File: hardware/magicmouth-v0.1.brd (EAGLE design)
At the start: 100 x 80 mm, 36 parts, among them IC1 LM386N, IC2 ATMEGA328P_PDIP, J2 AUDIO-JACK2PTH, Q1 16Mhz, U1 ARDUINOR3-NOIOREF-NOTEXT

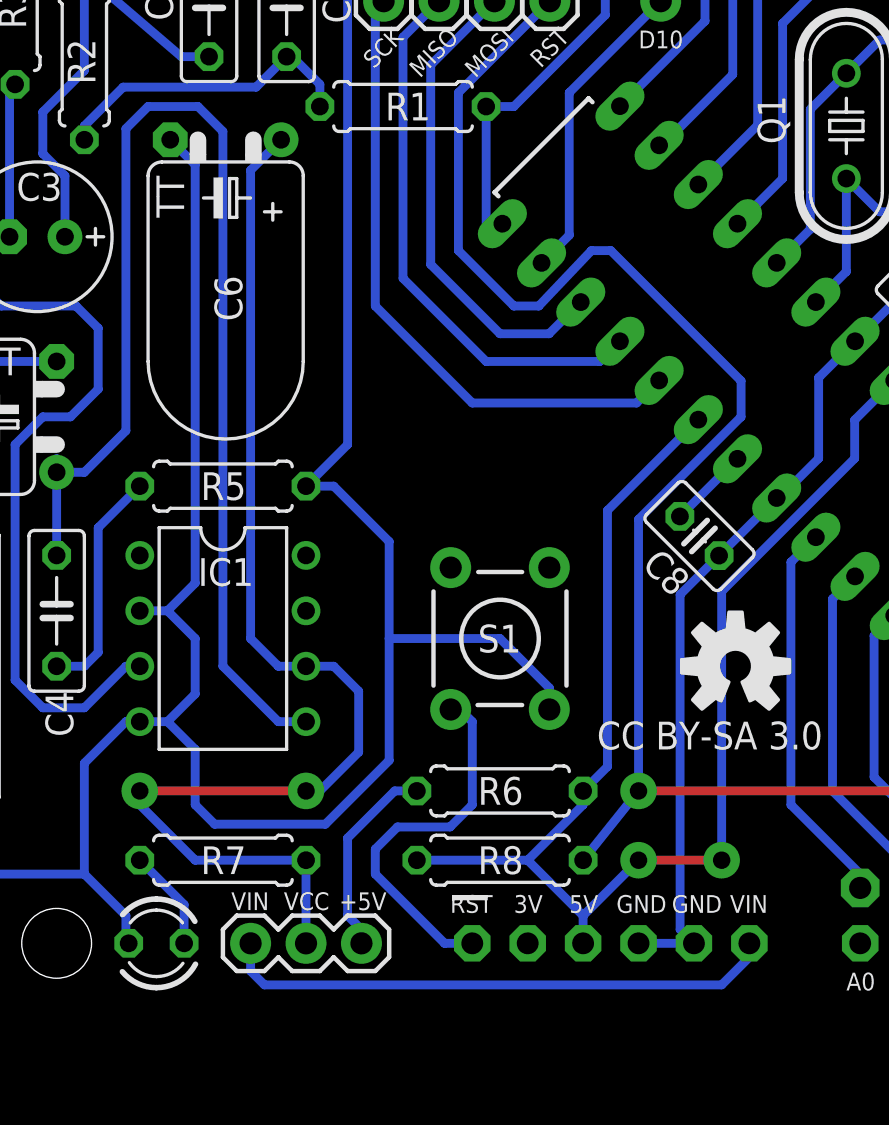
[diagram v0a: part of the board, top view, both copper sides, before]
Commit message: v0.1 and v1.0 eagle files
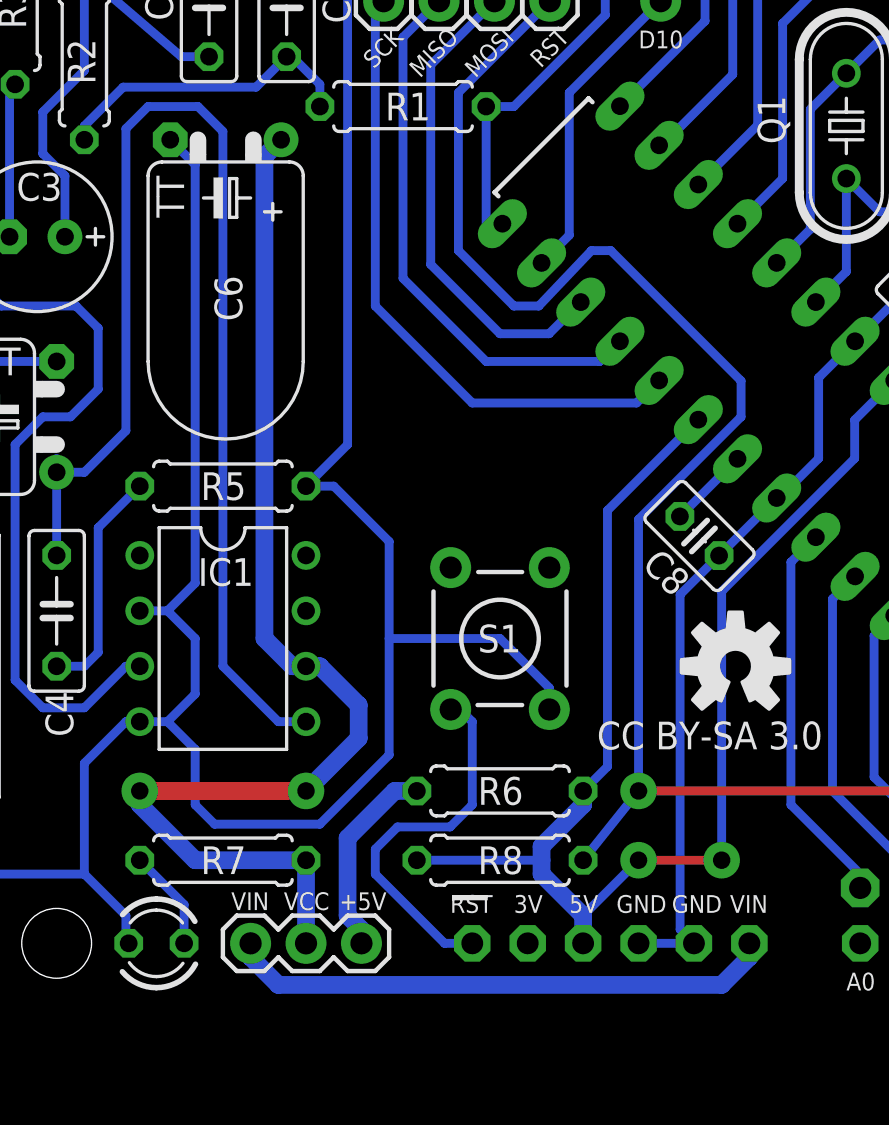
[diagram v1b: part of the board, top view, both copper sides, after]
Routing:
- net VCC: track 56.1 -> 54.4 mm
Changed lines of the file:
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@@
 <setting verticaltext="up"/>
 </settings>
-<grid distance="0.025" unitdist="inch" unit="mm" style="lines" multiple="1" display="yes" altdistance="0.025" altunitdist="inch" altunit="inch"/>
+<grid distance="25" unitdist="mil" unit="mil" style="lines" multiple="1" display="yes" altdistance="0.025" altunitdist="inch" altunit="inch"/>
 <layers>
 <layer number="1" name="Top" color="4" fill="1" visible="yes" active="yes"/>
@@
 <wire x1="27.305" y1="12.827" x2="27.432" y2="12.7" width="0.4064" layer="16"/>
 <wire x1="25.4" y1="15.875" x2="25.4" y2="20.955" width="0.4064" layer="16"/>
-<wire x1="36.449" y1="18.161" x2="39.37" y2="21.082" width="0.4064" layer="16"/>
+<wire x1="36.195" y1="18.161" x2="39.37" y2="21.336" width="0.4064" layer="16"/>
 <contactref element="R4" pad="A"/>
 <wire x1="27.305" y1="22.86" x2="27.94" y2="22.86" width="0.4064" layer="16"/>
@@
 <wire x1="30.48" y1="21.59" x2="30.48" y2="19.05" width="0.4064" layer="16"/>
 <wire x1="30.48" y1="19.05" x2="31.369" y2="18.161" width="0.4064" layer="16"/>
-<wire x1="31.369" y1="18.161" x2="36.449" y2="18.161" width="0.4064" layer="16"/>
+<wire x1="31.369" y1="18.161" x2="36.195" y2="18.161" width="0.4064" layer="16"/>
 <wire x1="25.4" y1="20.955" x2="27.305" y2="22.86" width="0.4064" layer="16"/>
 <contactref element="J1" pad="2"/>
@@
 <wire x1="36.83" y1="33.655" x2="39.37" y2="31.115" width="0.4064" layer="16"/>
 <wire x1="39.37" y1="31.115" x2="39.37" y2="26.67" width="0.4064" layer="16"/>
-<wire x1="39.37" y1="26.67" x2="39.37" y2="21.082" width="0.4064" layer="16"/>
+<wire x1="39.37" y1="26.67" x2="39.37" y2="21.336" width="0.4064" layer="16"/>
 <wire x1="35.56" y1="33.655" x2="35.433" y2="33.655" width="0.4064" layer="16"/>
 <wire x1="35.433" y1="33.655" x2="35.306" y2="33.782" width="0.4064" layer="16"/>
@@
 <contactref element="IC1" pad="6"/>
 <contactref element="C6" pad="+"/>
-<wire x1="36.83" y1="25.4" x2="35.56" y2="25.4" width="0.4064" layer="16"/>
-<wire x1="33.02" y1="48.133" x2="33.02" y2="26.67" width="0.4064" layer="16"/>
-<wire x1="33.02" y1="26.67" x2="34.29" y2="25.4" width="0.4064" layer="16"/>
-<wire x1="34.29" y1="25.4" x2="35.56" y2="25.4" width="0.4064" layer="16"/>
-<wire x1="37.973" y1="24.257" x2="36.83" y2="25.4" width="0.4064" layer="16"/>
-<wire x1="37.973" y1="24.257" x2="37.973" y2="21.463" width="0.4064" layer="16"/>
-<wire x1="35.56" y1="19.685" x2="36.195" y2="19.685" width="0.4064" layer="16"/>
-<wire x1="36.195" y1="19.685" x2="37.973" y2="21.463" width="0.4064" layer="16"/>
 <contactref element="R7" pad="2"/>
-<wire x1="30.48" y1="16.51" x2="27.94" y2="19.05" width="0.4064" layer="16"/>
-<wire x1="30.48" y1="16.51" x2="35.56" y2="16.51" width="0.4064" layer="16"/>
-<wire x1="35.56" y1="19.685" x2="27.94" y2="19.685" width="0.4064" layer="1"/>
-<wire x1="27.94" y1="19.685" x2="27.94" y2="19.05" width="0.4064" layer="16"/>
 <via x="35.56" y="19.685" extent="1-16" drill="0.8" diameter="1.6764"/>
 <via x="27.94" y="19.685" extent="1-16" drill="0.8" diameter="1.6764"/>
 <contactref element="JP1" pad="2"/>
-<wire x1="35.56" y1="12.7" x2="35.56" y2="16.51" width="0.4064" layer="16"/>
-<wire x1="33.02" y1="48.133" x2="34.417" y2="49.53" width="0.4064" layer="16"/>
+<wire x1="35.56" y1="25.4" x2="36.195" y2="25.4" width="0.8128" layer="16"/>
+<wire x1="36.195" y1="25.4" x2="37.973" y2="23.622" width="0.8128" layer="16"/>
+<wire x1="37.973" y1="23.622" x2="37.973" y2="22.098" width="0.8128" layer="16"/>
+<wire x1="37.973" y1="22.098" x2="35.56" y2="19.685" width="0.8128" layer="16"/>
+<wire x1="35.56" y1="12.7" x2="35.56" y2="16.51" width="0.8128" layer="16"/>
+<wire x1="35.56" y1="16.51" x2="30.48" y2="16.51" width="0.8128" layer="16"/>
+<wire x1="30.48" y1="16.51" x2="27.94" y2="19.05" width="0.8128" layer="16"/>
+<wire x1="27.94" y1="19.05" x2="27.94" y2="19.685" width="0.8128" layer="16"/>
+<wire x1="27.94" y1="19.685" x2="35.56" y2="19.685" width="0.8128" layer="1"/>
+<wire x1="35.56" y1="25.4" x2="34.925" y2="25.4" width="0.8128" layer="16"/>
+<wire x1="34.925" y1="25.4" x2="33.655" y2="26.67" width="0.8128" layer="16"/>
+<wire x1="33.655" y1="26.67" x2="33.655" y2="48.768" width="0.8128" layer="16"/>
+<wire x1="33.655" y1="48.768" x2="34.417" y2="49.53" width="0.8128" layer="16"/>
 </signal>
 <signal name="N$7">
 <contactref element="R6" pad="1"/>
-<wire x1="38.1" y1="13.335" x2="37.465" y2="13.97" width="0.4064" layer="16"/>
-<wire x1="37.465" y1="13.97" x2="37.465" y2="17.526" width="0.4064" layer="16"/>
-<wire x1="37.465" y1="17.526" x2="39.624" y2="19.685" width="0.4064" layer="16"/>
-<wire x1="39.624" y1="19.685" x2="40.64" y2="19.685" width="0.4064" layer="16"/>
 <contactref element="JP1" pad="1"/>
-<wire x1="38.1" y1="12.7" x2="38.1" y2="13.335" width="0.4064" layer="16"/>
+<wire x1="38.1" y1="12.7" x2="38.1" y2="13.335" width="0.8128" layer="16"/>
+<wire x1="38.1" y1="13.335" x2="37.465" y2="13.97" width="0.8128" layer="16"/>
+<wire x1="37.465" y1="13.97" x2="37.465" y2="17.526" width="0.8128" layer="16"/>
+<wire x1="37.465" y1="17.526" x2="39.624" y2="19.685" width="0.8128" layer="16"/>
+<wire x1="39.624" y1="19.685" x2="40.64" y2="19.685" width="0.8128" layer="16"/>
 </signal>
 <signal name="N$10">
@@
 <wire x1="54.61" y1="28.829" x2="60.706" y2="34.925" width="0.4064" layer="16"/>
 <wire x1="60.706" y1="34.925" x2="60.706" y2="36.68495" width="0.4064" layer="16"/>
-<wire x1="48.26" y1="12.7" x2="48.26" y2="13.97" width="0.4064" layer="16"/>
 <wire x1="48.26" y1="13.97" x2="50.8" y2="16.51" width="0.4064" layer="16"/>
 <wire x1="50.8" y1="16.51" x2="54.61" y2="16.51" width="0.4064" layer="1"/>
@@
 <via x="50.8" y="16.51" extent="1-16" drill="0.8" diameter="1.6764"/>
 <via x="54.61" y="16.51" extent="1-16" drill="0.8" diameter="1.6764"/>
-<wire x1="45.72" y1="16.51" x2="48.26" y2="13.97" width="0.4064" layer="16"/>
-<wire x1="48.26" y1="19.685" x2="48.26" y2="19.05" width="0.4064" layer="16"/>
-<wire x1="48.26" y1="19.05" x2="45.72" y2="16.51" width="0.4064" layer="16"/>
 <wire x1="49.375921875" y1="32.539078125" x2="49.375921875" y2="20.800921875" width="0.4064" layer="16"/>
 <wire x1="49.375921875" y1="20.800921875" x2="48.26" y2="19.685" width="0.4064" layer="16"/>
@@
 <contactref element="R8" pad="2"/>
 <contactref element="IC2" pad="20"/>
-<wire x1="40.64" y1="16.51" x2="45.72" y2="16.51" width="0.4064" layer="16"/>
 <wire x1="53.53984375" y1="36.703" x2="49.375921875" y2="32.539078125" width="0.4064" layer="16"/>
 <contactref element="IC2" pad="7"/>
@@
 <wire x1="62.5201" y1="38.49905" x2="62.647103125" y2="38.49905" width="0.4064" layer="16"/>
 <wire x1="62.647103125" y1="38.49905" x2="65.096525" y2="40.948471875" width="0.4064" layer="16"/>
+<wire x1="48.26" y1="12.7" x2="48.26" y2="13.97" width="0.8128" layer="16"/>
+<wire x1="48.26" y1="19.05" x2="48.26" y2="19.685" width="0.8128" layer="16"/>
+<wire x1="48.26" y1="19.05" x2="46.355" y2="17.145" width="0.8128" layer="16"/>
+<wire x1="46.355" y1="17.145" x2="46.355" y2="16.51" width="0.8128" layer="16"/>
+<wire x1="46.355" y1="16.51" x2="46.355" y2="15.875" width="0.8128" layer="16"/>
+<wire x1="46.355" y1="15.875" x2="48.26" y2="13.97" width="0.8128" layer="16"/>
+<wire x1="40.64" y1="16.51" x2="46.355" y2="16.51" width="0.4064" layer="16"/>
 </signal>
 <signal name="GND1">
@@
 <signal name="VIN">
 <contactref element="U1" pad="VIN"/>
-<wire x1="55.88" y1="12.7" x2="55.88" y2="12.065" width="0.4064" layer="16"/>
-<wire x1="55.88" y1="12.065" x2="54.61" y2="10.795" width="0.4064" layer="16"/>
-<wire x1="54.61" y1="10.795" x2="33.655" y2="10.795" width="0.4064" layer="16"/>
-<wire x1="33.655" y1="10.795" x2="33.02" y2="11.43" width="0.4064" layer="16"/>
 <contactref element="JP1" pad="3"/>
-<wire x1="33.02" y1="12.7" x2="33.02" y2="11.43" width="0.4064" layer="16"/>
+<wire x1="33.02" y1="12.7" x2="33.02" y2="12.065" width="0.8128" layer="16"/>
+<wire x1="33.02" y1="12.065" x2="34.29" y2="10.795" width="0.8128" layer="16"/>
+<wire x1="34.29" y1="10.795" x2="54.61" y2="10.795" width="0.8128" layer="16"/>
+<wire x1="54.61" y1="10.795" x2="55.88" y2="12.065" width="0.8128" layer="16"/>
+<wire x1="55.88" y1="12.065" x2="55.88" y2="12.7" width="0.8128" layer="16"/>
 </signal>
 <signal name="N$34">
